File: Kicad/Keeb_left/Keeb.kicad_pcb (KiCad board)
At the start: 2 copper layers, 118 x 118 mm, 23 parts, among them J1 MJ-4PP-9, SW1 CherryMX, SW10 CherryMX, SW11 CherryMX, SW12 CherryMX, SW13 CherryMX, SW14 CherryMX, SW15 CherryMX, SW16 CherryMX, SW17 CherryMX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

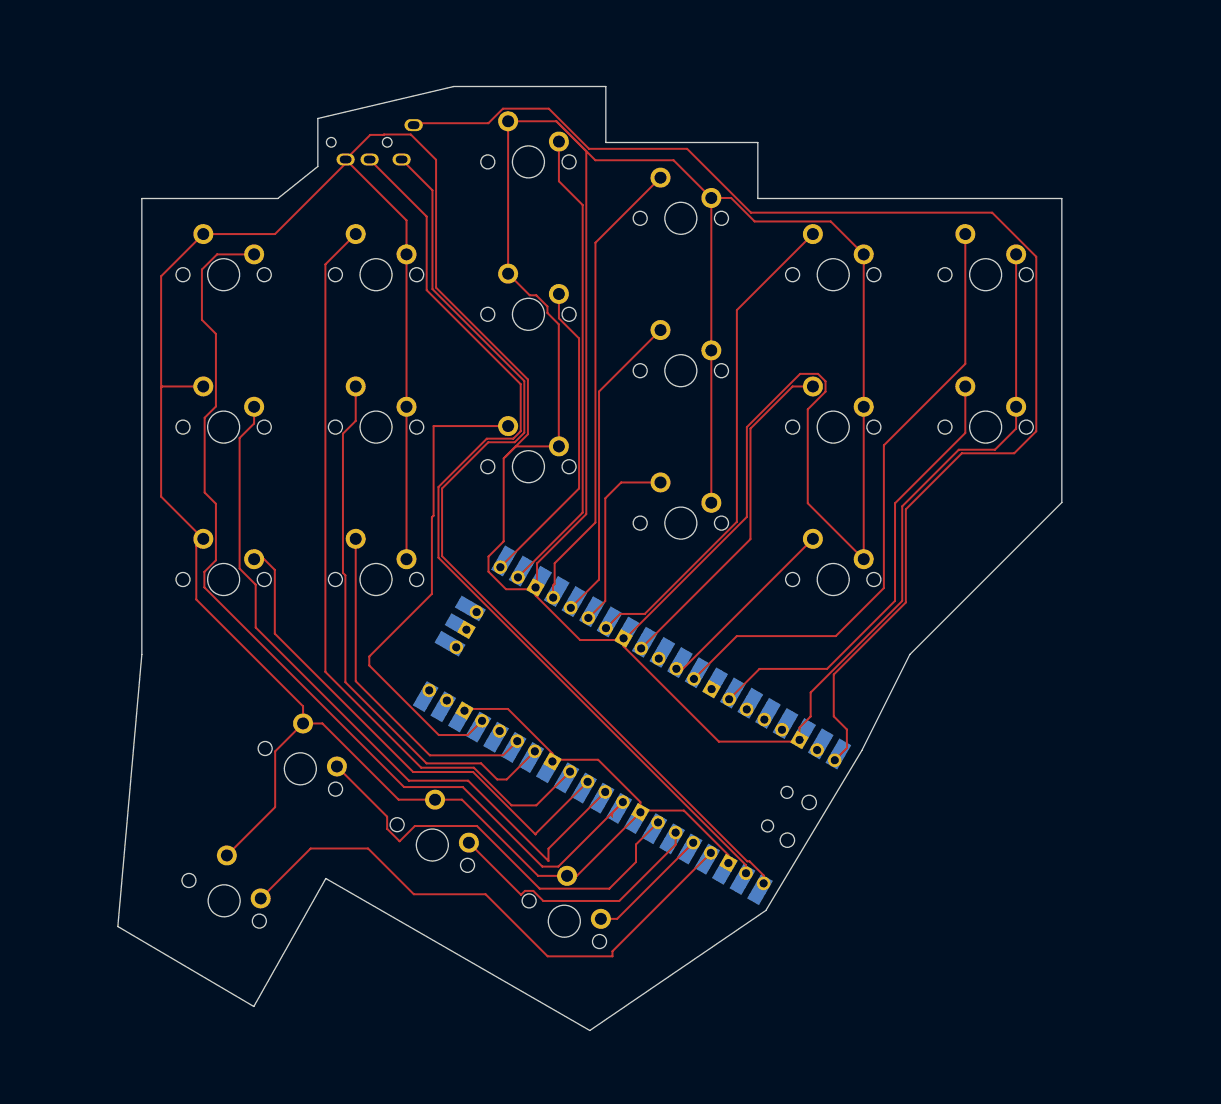
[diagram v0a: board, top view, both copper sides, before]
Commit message: spaced out tracks
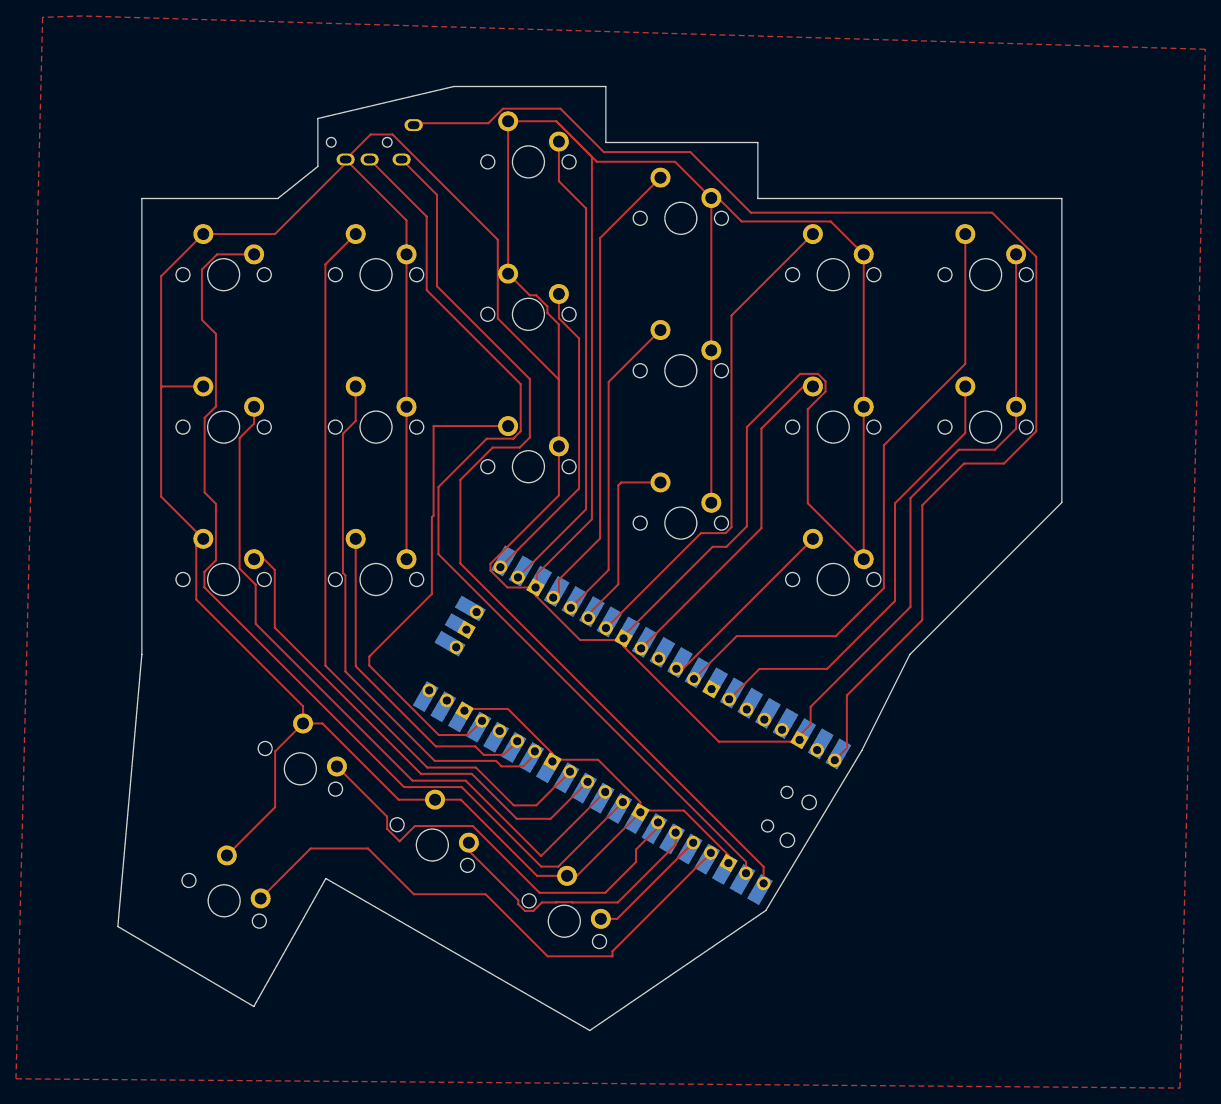
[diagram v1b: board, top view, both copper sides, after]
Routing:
- net GND: track 778.0 -> 773.4 mm
- net 3v3: track 164.9 -> 162.6 mm
- net 8: track 63.4 -> 61.3 mm
- net 10: track 67.9 -> 66.0 mm
- net 7: track 89.4 -> 87.8 mm
- net 4: track 33.7 -> 35.2 mm
- net 0: track 119.9 -> 118.4 mm
- net 11: track 42.6 -> 41.5 mm
- net 22: track 43.1 -> 42.3 mm
- added copper zone on F.Cu, net (none)
